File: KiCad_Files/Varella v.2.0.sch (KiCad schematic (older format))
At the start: 28 parts, among them J1 ESQ-120-39-G-D, J2 Conn_01x12_Male, U1 STM32L476RGTx, Y1 32,768k

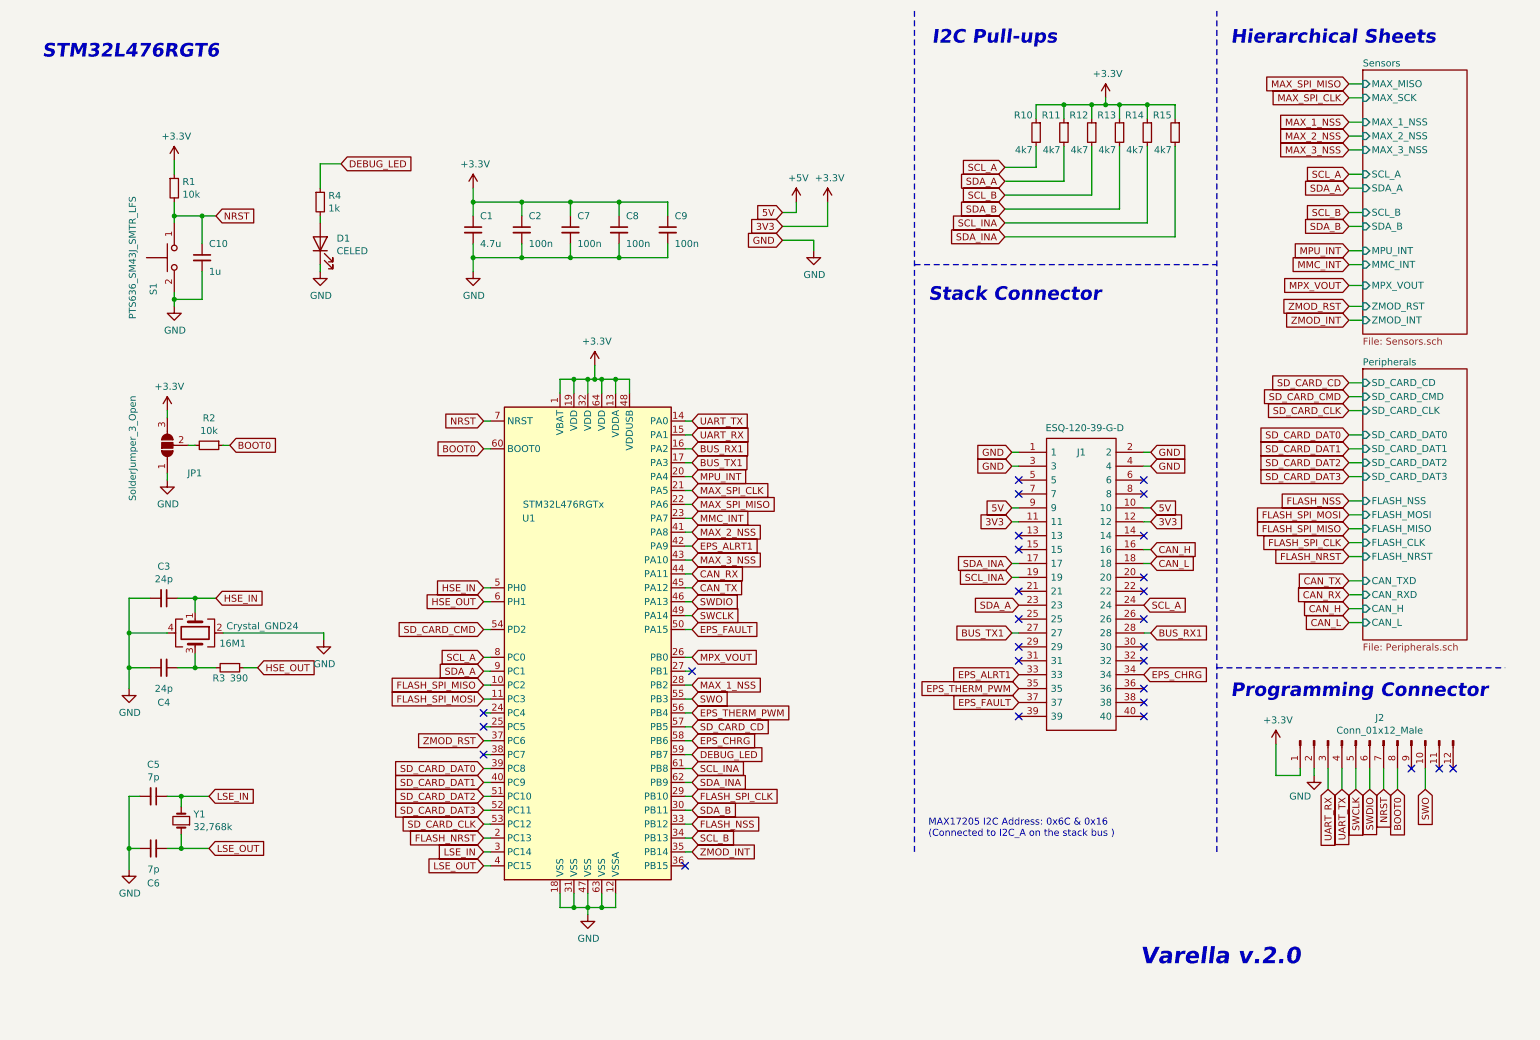
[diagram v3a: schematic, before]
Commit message: Update RTC Battery Silk Screen name
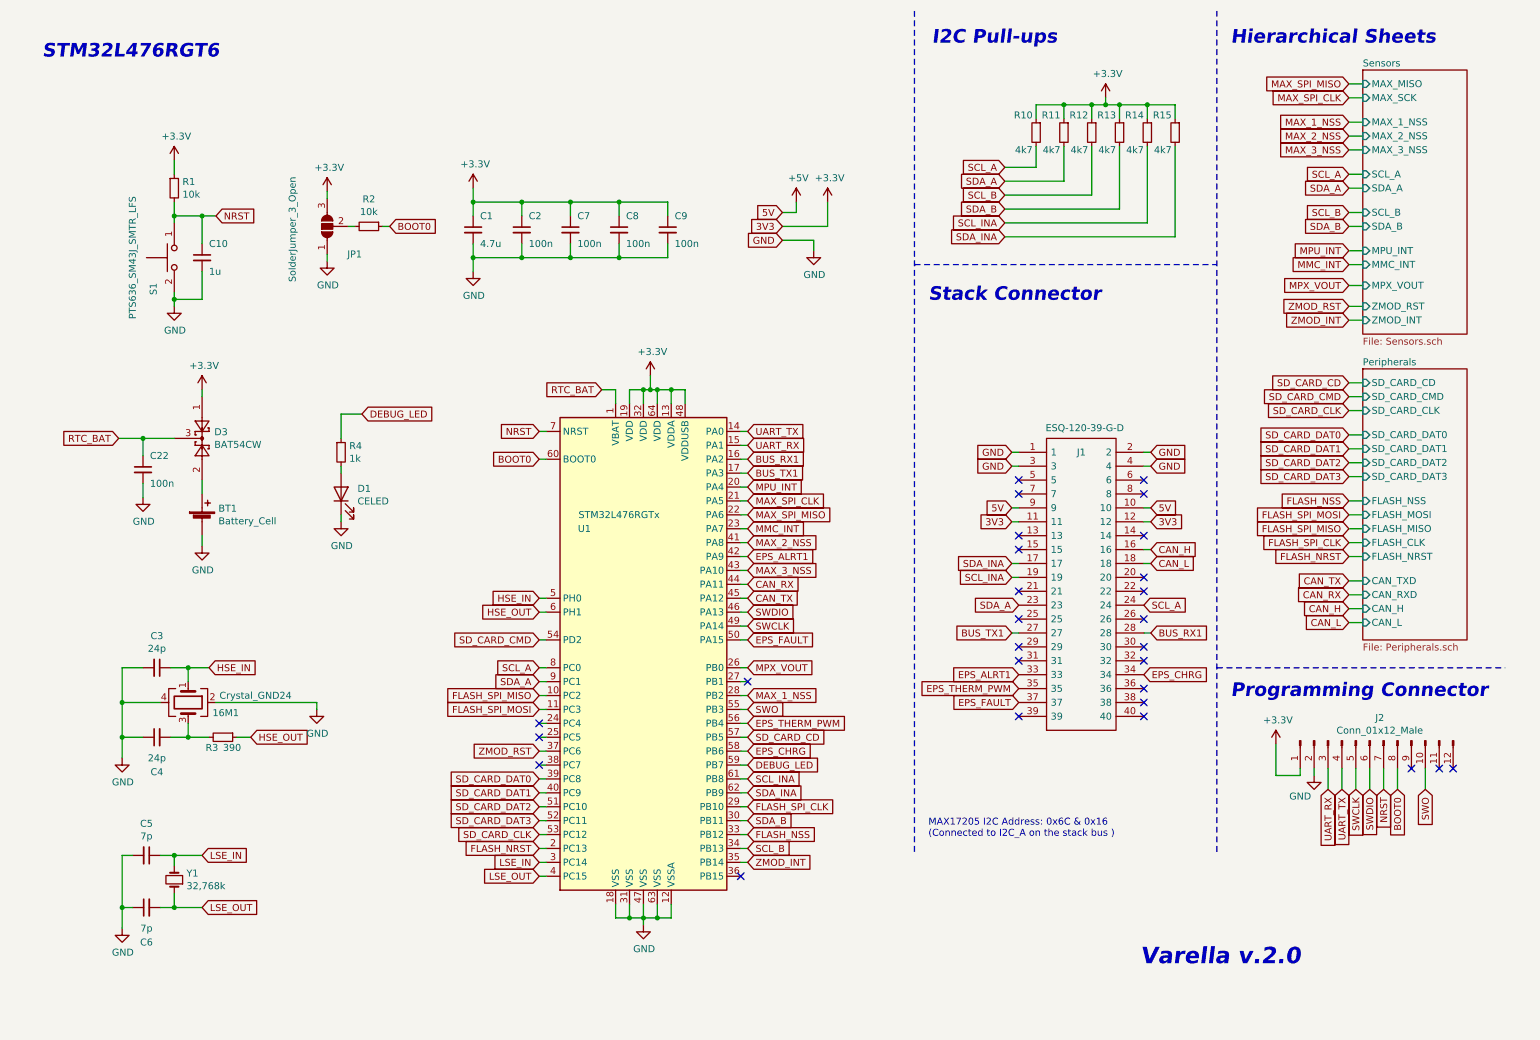
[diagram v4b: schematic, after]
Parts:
- added BT1: Battery_Cell, SamacSys_Parts:3030, symbol Device:Battery_Cell
- added C22: 100n, Capacitor_SMD:C_0603_1608Metric, symbol archive:Device_C_Small
- added D3: BAT54CW, Package_TO_SOT_SMD:SOT-323_SC-70, symbol Diode:BAT54CW
- C9: footprint Capacitor_SMD:C_0805_2012Metric -> Capacitor_SMD:C_0603_1608Metric
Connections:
- net +3V3: now also D3.1; no longer U1.1 (VBAT)
- net GND: now also BT1.2 (-), C22.2
- new net: BT1.1 (+), D3.2
- new net RTC_BAT: C22.1, D3.3, U1.1 (VBAT)
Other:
- moved on the sheet: 16M1, C3, C4, C5, C6, D1, JP1, R2, R3, R4, U1, Y1

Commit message: Add 1,024 V voltage reference for the ADC.
We realised that the MPX5700 barometer would only output a voltage from 0 to 0,66 V in the altitude range of the radiosonde trajectory. By adding this voltage reference to the ADC we will have much better precision on pressure readings.
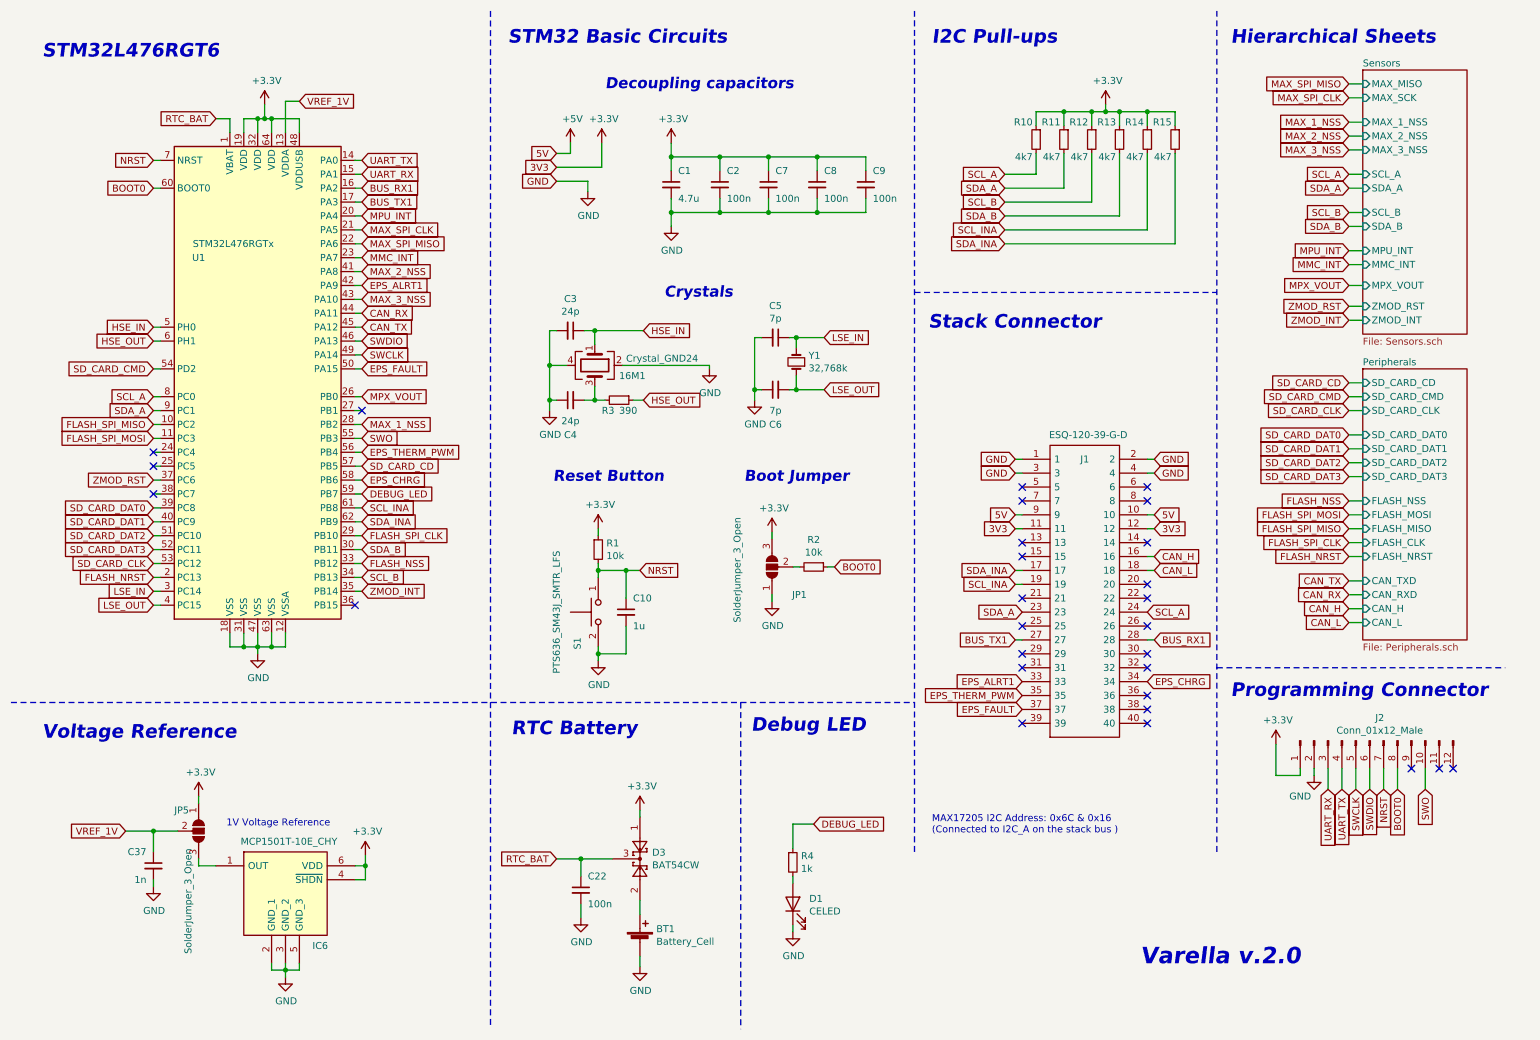
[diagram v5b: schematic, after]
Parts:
- added C37: 1n, Capacitor_SMD:C_0603_1608Metric, symbol archive:Device_C_Small
- added IC6: MCP1501T-10E_CHY, SamacSys_Parts:SOT95P280X145-6N, symbol SamacSys_Parts:MCP1501T-10E_CHY
- added JP5: SolderJumper_3_Open, Jumper:SolderJumper-3_P1.3mm_Open_RoundedPad1.0x1.5mm_NumberLabels, symbol Jumper:SolderJumper_3_Open
- C8: footprint Capacitor_SMD:C_0805_2012Metric -> Capacitor_SMD:C_0603_1608Metric
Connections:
- net +3V3: now also IC6.4 (~SHDN), IC6.6 (VDD), JP5.1 (A); no longer U1.13 (VDDA)
- net GND: now also C37.2, IC6.2 (GND_1), IC6.3 (GND_2), IC6.5 (GND_3)
- new net: IC6.1 (OUT), JP5.3 (B)
- new net VREF_1V: C37.1, JP5.2 (C), U1.13 (VDDA)
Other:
- note added: "1V Voltage Reference"
- note added: "Boot Jumper"
- note added: "Crystals"
- note added: "Debug LED\n"
- note added: "Decoupling capacitors"
- note added: "RTC Battery"
- note added: "Reset Button\n"
- note added: "STM32 Basic Circuits"
- note added: "Voltage Reference"
- moved on the sheet: 16M1, BT1, C1, C10, C2, C22, C3, C4, C5, C6, C7, C8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
